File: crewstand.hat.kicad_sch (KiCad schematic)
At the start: 17 parts, among them J1 GPIO, J2 CAN Terminal, J3 Sensor Terminal, J4 V-In, J5 Relais Out, J6 V-Out, U2 MCP2515-xSO, U3 MCP2551-I-P, U4 PicoW, Y2 12M

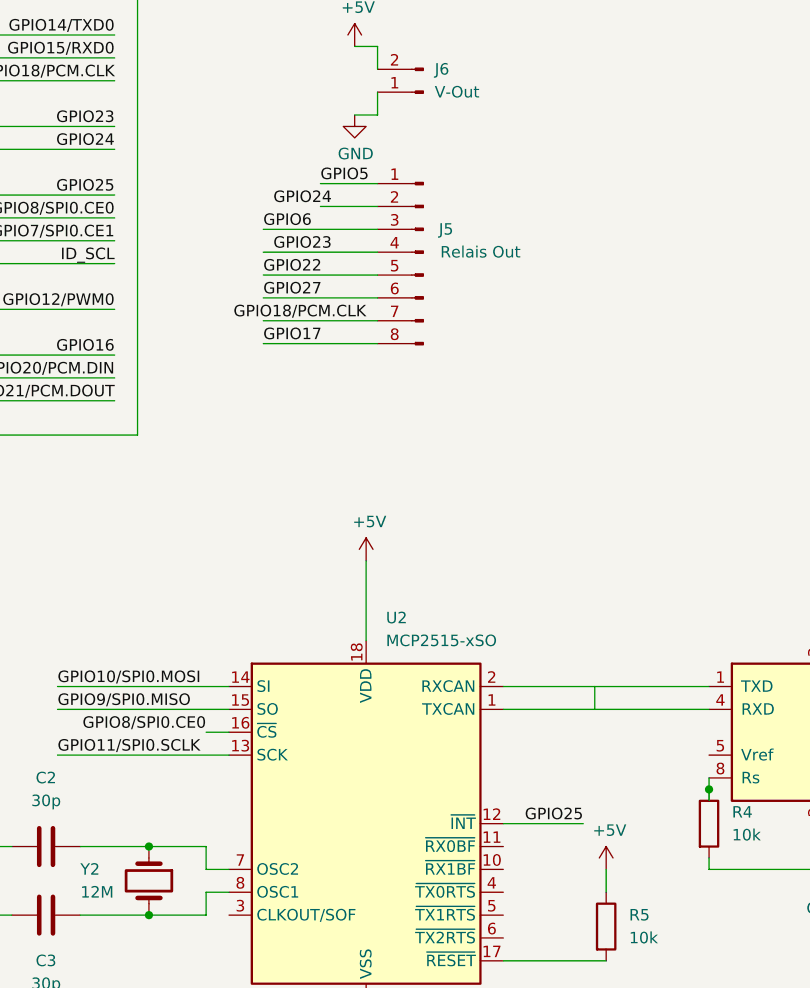
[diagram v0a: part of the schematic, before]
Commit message: feat: use jst connectors
* update clearance and track width
* Optimize placement and tracks

issue #2
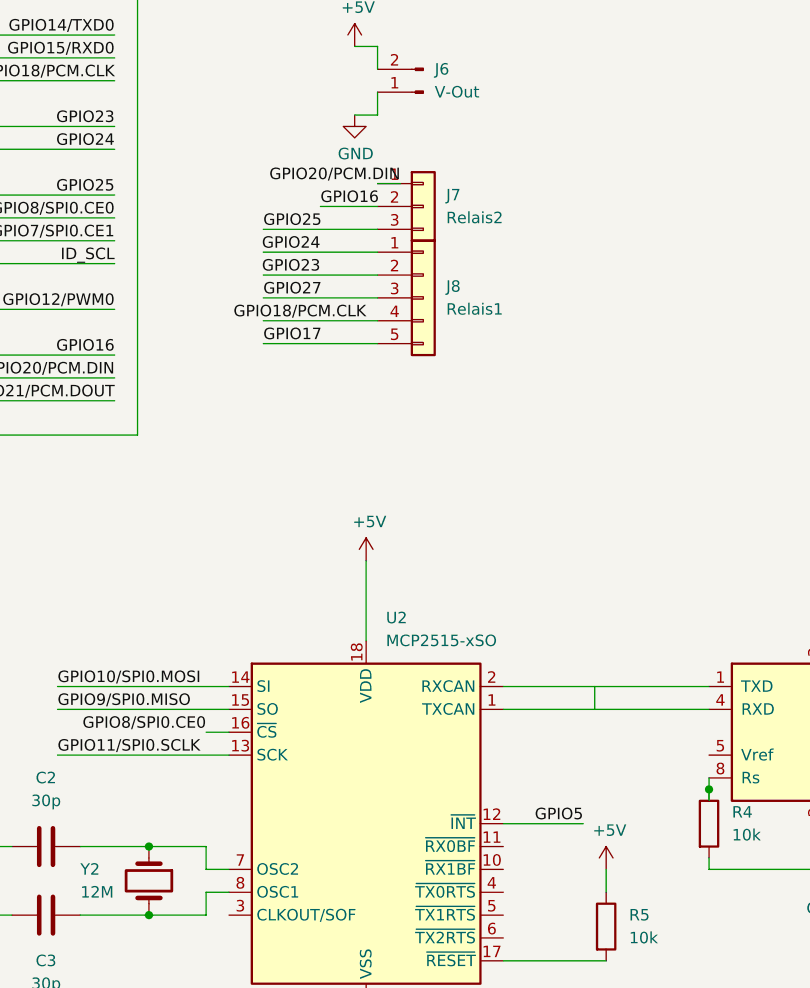
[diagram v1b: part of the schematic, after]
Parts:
- removed J5: Relais Out, Connector_JST:JST_EH_B8B-EH-A_1x08_P2.50mm_Vertical, symbol Connector:Conn_01x08_Pin
- added J7: Relais2, Connector_JST:JST_XH_B3B-XH-A_1x03_P2.50mm_Vertical, symbol Connector_Generic:Conn_01x03
- added J8: Relais1, Connector_JST:JST_XH_B5B-XH-A_1x05_P2.50mm_Vertical, symbol Connector_Generic:Conn_01x05
- J6: footprint Connector_JST:JST_EH_B2B-EH-A_1x02_P2.50mm_Vertical -> Connector_JST:JST_XH_B2B-XH-A_1x02_P2.50mm_Vertical
- U4: footprint RaspberryPi:RPi_PicoW_SMD_TH -> RaspberryPI PicoW:RPi_PicoW_SMD_TH
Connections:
- net GPIO16: now also J7.2 (Pin_2)
- net GPIO17: now also J8.5 (Pin_5)
- net GPIO18/PCM.CLK: now also J8.4 (Pin_4)
- net GPIO20/PCM.DIN: now also J7.1 (Pin_1)
- net GPIO23: now also J8.2 (Pin_2)
- net GPIO24: now also J8.1 (Pin_1)
- net GPIO25: now also J7.3 (Pin_3); no longer U2.12 (~{INT})
- net GPIO27: now also J8.3 (Pin_3)
- net GPIO5: now also U2.12 (~{INT})
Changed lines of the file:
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@@
     (stroke (width 0) (type default))
   )
-  (wire (pts (xy 123.19 52.07) (xy 129.54 52.07))
+  (wire (pts (xy 132.08 52.07) (xy 129.54 52.07))
     (stroke (width 0) (type default))
   )
@@
     (effects (font (size 1.27 1.27)) (justify right bottom))
   )
+  (label "GPIO25" (at 116.84 57.15 0) (fields_autoplaced)
+    (effects (font (size 1.27 1.27)) (justify left bottom))
+  )
+  (label "GPIO24" (at 123.19 59.69 180) (fields_autoplaced)
+    (effects (font (size 1.27 1.27)) (justify right bottom))
+  )
   (label "GPIO16" (at 100.33 71.12 180) (fields_autoplaced)
     (effects (font (size 1.27 1.27)) (justify right bottom))
   )
-  (label "GPIO6" (at 116.84 57.15 0) (fields_autoplaced)
-    (effects (font (size 1.27 1.27)) (justify left bottom))
-  )
   (label "GPIO11{slash}SPI0.SCLK" (at 93.98 115.57 0) (fields_autoplaced)
     (effects (font (size 1.27 1.27)) (justify left bottom))
@@
     (effects (font (size 1.27 1.27)) (justify left bottom))
   )
+  (label "GPIO20{slash}PCM.DIN" (at 132.08 52.07 180) (fields_autoplaced)
+    (effects (font (size 1.27 1.27)) (justify right bottom))
+  )
   (label "GPIO17" (at 31.75 40.64 0) (fields_autoplaced)
     (effects (font (size 1.27 1.27)) (justify left bottom))
   )
+  (label "GPIO16" (at 123.19 54.61 0) (fields_autoplaced)
+    (effects (font (size 1.27 1.27)) (justify left bottom))
+  )
   (label "GPIO25" (at 100.33 53.34 180) (fields_autoplaced)
     (effects (font (size 1.27 1.27)) (justify right bottom))
   )
+  (label "GPIO23" (at 123.19 62.23 180) (fields_autoplaced)
+    (effects (font (size 1.27 1.27)) (justify right bottom))
+  )
   (label "GPIO3{slash}SCL1" (at 31.75 33.02 0) (fields_autoplaced)
     (effects (font (size 1.27 1.27)) (justify left bottom))
@@
     (effects (font (size 1.27 1.27)) (justify right bottom))
   )
-  (label "GPIO23" (at 124.46 59.69 180) (fields_autoplaced)
-    (effects (font (size 1.27 1.27)) (justify right bottom))
-  )
   (label "ADC0" (at 254 52.07 180) (fields_autoplaced)
     (effects (font (size 1.27 1.27)) (justify right bottom))
@@
     (effects (font (size 1.27 1.27)) (justify left bottom))
   )
-  (label "GPIO5" (at 123.19 52.07 0) (fields_autoplaced)
-    (effects (font (size 1.27 1.27)) (justify left bottom))
-  )
   (label "GPIO20{slash}PCM.DIN" (at 100.33 73.66 180) (fields_autoplaced)
     (effects (font (size 1.27 1.27)) (justify right bottom))
@@
     (effects (font (size 1.27 1.27)) (justify right bottom))
   )
-  (label "GPIO22" (at 116.84 62.23 0) (fields_autoplaced)
-    (effects (font (size 1.27 1.27)) (justify left bottom))
-  )
   (label "GPIO7{slash}SPI0.CE1" (at 100.33 58.42 180) (fields_autoplaced)
     (effects (font (size 1.27 1.27)) (justify right bottom))
@@
     (effects (font (size 1.27 1.27)) (justify right bottom))
   )
-  (label "GPIO24" (at 124.46 54.61 180) (fields_autoplaced)
-    (effects (font (size 1.27 1.27)) (justify right bottom))
-  )
   (label "GPIO15{slash}RXD0" (at 257.81 77.47 180) (fields_autoplaced)
     (effects (font (size 1.27 1.27)) (justify right bottom))
@@
     (effects (font (size 1.27 1.27)) (justify left bottom))
   )
-  (label "GPIO25" (at 152.4 123.19 180) (fields_autoplaced)
+  (label "GPIO5" (at 152.4 123.19 180) (fields_autoplaced)
     (effects (font (size 1.27 1.27)) (justify right bottom))
   )
@@
       (effects (font (size 1.27 1.27)))
     )
-    (property "Footprint" "RaspberryPi:RPi_PicoW_SMD_TH" (at 220.98 53.34 90)
+    (property "Footprint" "RaspberryPI PicoW:RPi_PicoW_SMD_TH" (at 220.98 53.34 90)
       (effects (font (size 1.27 1.27)) hide)
     )
@@
     )
   )
+  (symbol (lib_id "Connector_Generic:Conn_01x05") (at 134.62 64.77 0) (unit 1)
+    (in_bom yes) (on_board yes) (dnp no) (fields_autoplaced)
+    (property "Reference" "J8" (at 137.16 63.5 0)
+      (effects (font (size 1.27 1.27)) (justify left))
+    )
+    (property "Value" "Relais1" (at 137.16 66.04 0)
+      (effects (font (size 1.27 1.27)) (justify left))
+    )
+    (property "Footprint" "Connector_JST:JST_XH_B5B-XH-A_1x05_P2.50mm_Vertical" (at 134.62 64.77 0)
+      (effects (font (size 1.27 1.27)) hide)
+    )
+    (property "Datasheet" "~" (at 134.62 64.77 0)
+      (effects (font (size 1.27 1.27)) hide)
+    )
+    (pin "2")
+    (pin "1")
+    (pin "4")
+    (pin "3")
+    (pin "5")
+    (instances
+      (project "crewstand.hat"
+        (path "/e63e39d7-6ac0-4ffd-8aa3-1841a4541b55"
+          (reference "J8") (unit 1)
+        )
+      )
+    )
+  )
   (symbol (lib_id "Device:R") (at 257.81 52.07 90) (unit 1)
     (in_bom yes) (on_board yes) (dnp no)
@@
     )
   )
-  (symbol (lib_id "Connector:Conn_01x08_Pin") (at 134.62 59.69 0) (mirror y) (unit 1)
-    (in_bom yes) (on_board yes) (dnp no)
-    (property "Reference" "J5" (at 137.16 57.15 0)
-      (effects (font (size 1.27 1.27)))
-    )
-    (property "Value" "Relais Out" (at 140.97 59.69 0)
-      (effects (font (size 1.27 1.27)))
-    )
-    (property "Footprint" "Connector_JST:JST_EH_B8B-EH-A_1x08_P2.50mm_Vertical" (at 134.62 59.69 0)
-      (effects (font (size 1.27 1.27)) hide)
-    )
-    (property "Datasheet" "~" (at 134.62 59.69 0)
-      (effects (font (size 1.27 1.27)) hide)
-    )
-    (pin "5")
-    (pin "8")
-    (pin "2")
-    (pin "1")
-    (pin "3")
-    (pin "4")
-    (pin "7")
-    (pin "6")
-    (instances
-      (project "crewstand.hat"
-        (path "/e63e39d7-6ac0-4ffd-8aa3-1841a4541b55"
-          (reference "J5") (unit 1)
-        )
-      )
-    )
-  )
   (symbol (lib_id "power:GND") (at 127 44.45 0) (unit 1)
     (in_bom yes) (on_board yes) (dnp no)
@@
     )
   )
+  (symbol (lib_id "Connector_Generic:Conn_01x03") (at 134.62 54.61 0) (unit 1)
+    (in_bom yes) (on_board yes) (dnp no) (fields_autoplaced)
+    (property "Reference" "J7" (at 137.16 53.34 0)
+      (effects (font (size 1.27 1.27)) (justify left))
+    )
+    (property "Value" "Relais2" (at 137.16 55.88 0)
+      (effects (font (size 1.27 1.27)) (justify left))
+    )
+    (property "Footprint" "Connector_JST:JST_XH_B3B-XH-A_1x03_P2.50mm_Vertical" (at 134.62 54.61 0)
+      (effects (font (size 1.27 1.27)) hide)
+    )
+    (property "Datasheet" "~" (at 134.62 54.61 0)
+      (effects (font (size 1.27 1.27)) hide)
+    )
+    (pin "1")
+    (pin "3")
+    (pin "2")
+    (instances
+      (project "crewstand.hat"
+        (path "/e63e39d7-6ac0-4ffd-8aa3-1841a4541b55"
+          (reference "J7") (unit 1)
+        )
+      )
+    )
+  )
   (symbol (lib_id "power:GND") (at 220.98 83.82 0) (mirror y) (unit 1)
     (in_bom yes) (on_board yes) (dnp no)
@@
       (effects (font (size 1.27 1.27)) (justify right))
     )
-    (property "Footprint" "Connector_JST:JST_EH_B2B-EH-A_1x02_P2.50mm_Vertical" (at 134.62 41.91 0)
-      (effects (font (size 1.27 1.27)) hide)
-    )
+    (property "Footprint" "Connector_JST:JST_XH_B2B-XH-A_1x02_P2.50mm_Vertical" (at 134.62 41.91 0)
+      (effects (font (size 1.27 1.27)) hide)
+    )
